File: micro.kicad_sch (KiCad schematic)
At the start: 29 parts, among them J7 USB_C_Receptacle_USB2.0_16P, J8 Conn_01x04_Pin, J9 Conn_01x06_Pin, SW2 SW_Push, U4 STM32F411RETx, U5 TME-0505S, U6 ADUM3160

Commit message: aggiunto oscillatore allo schematico
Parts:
- added C49, C50: 100n, Capacitor_SMD:C_0603_1608Metric, symbol Device:C
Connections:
- net +3V3: now also C49.1, C50.1
- net GND: now also C49.2, C50.2
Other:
- moved on the sheet: C45, C48, SW2

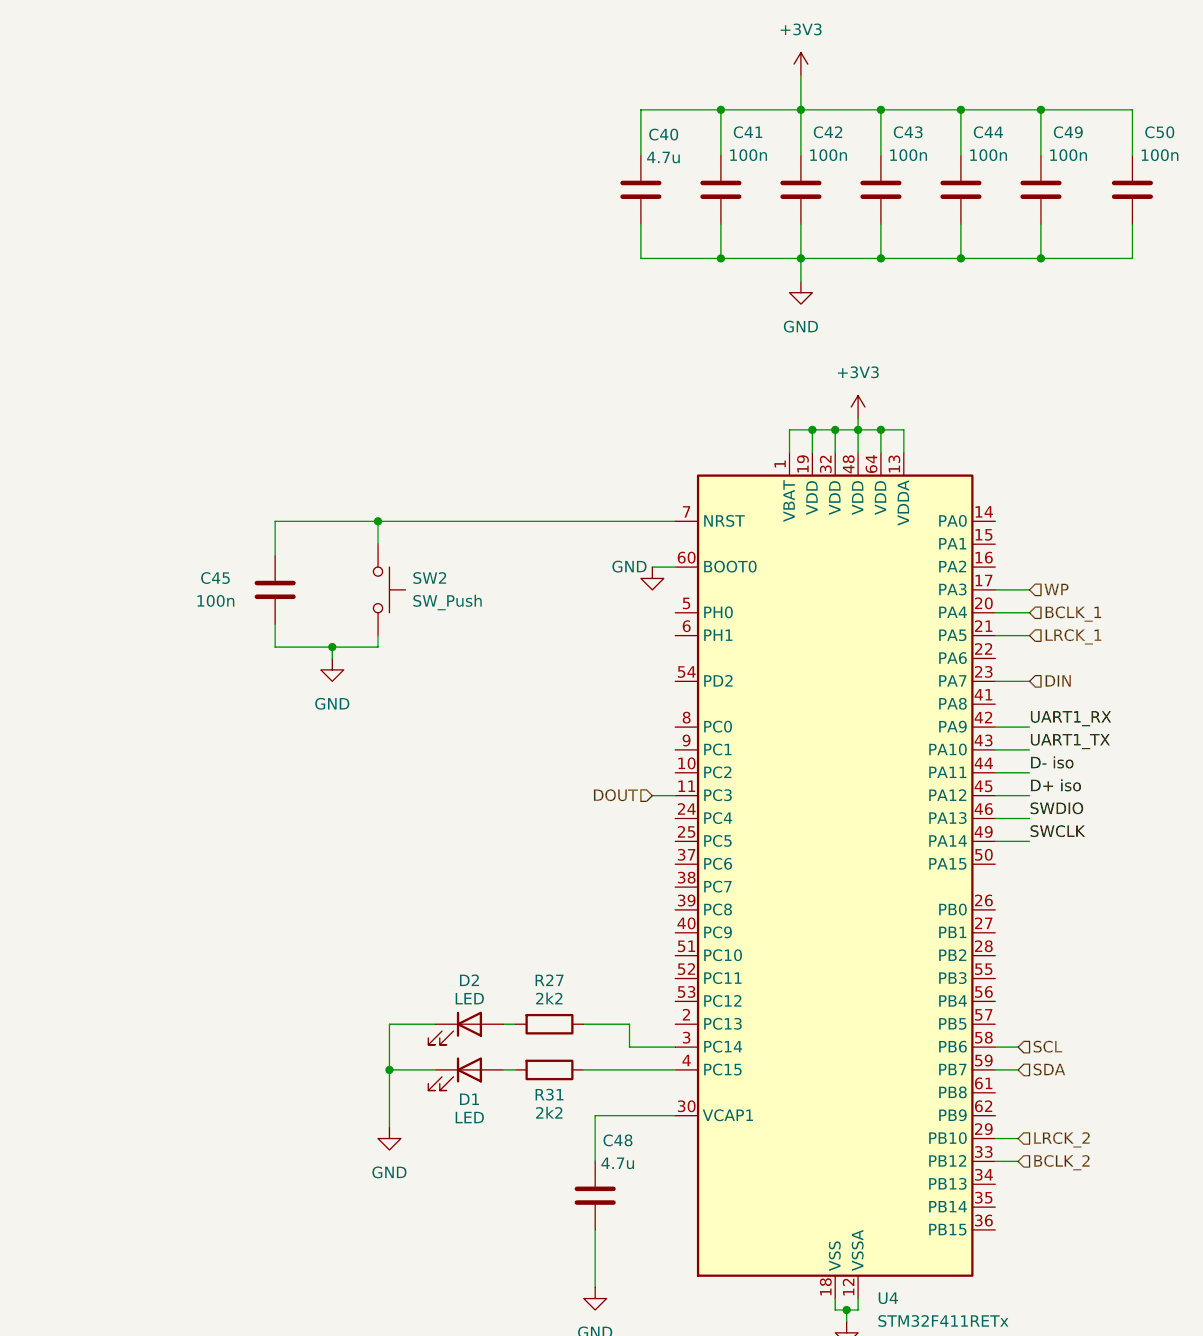
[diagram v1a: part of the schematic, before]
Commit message: sostituito dei componenti non piu disponibili
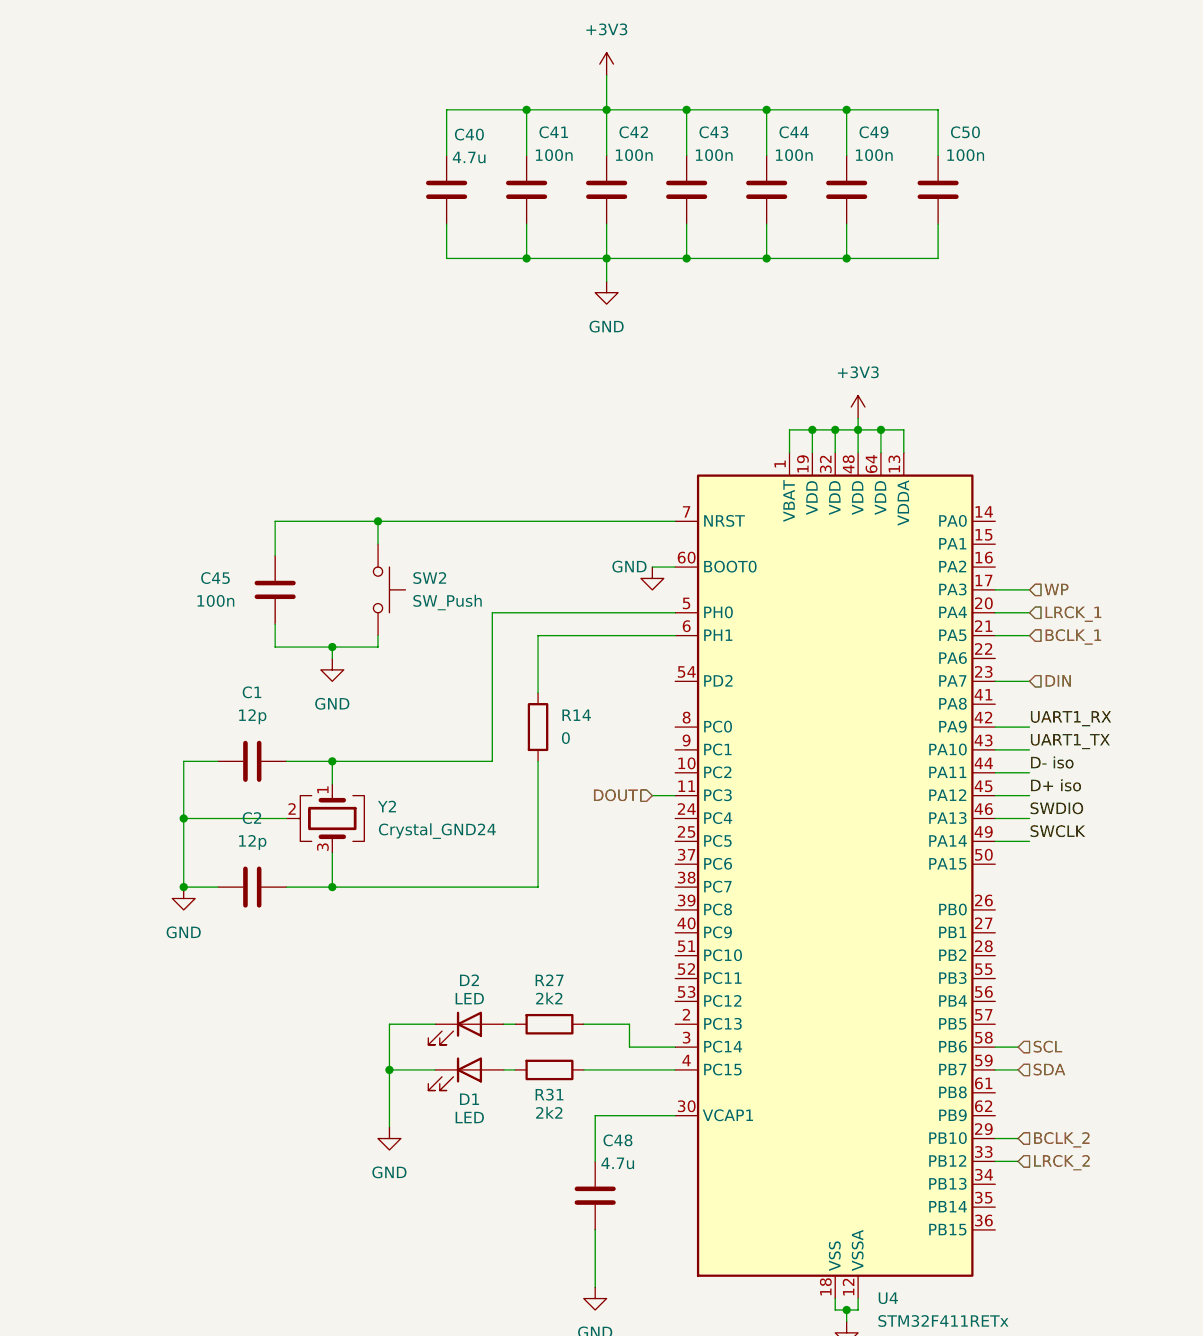
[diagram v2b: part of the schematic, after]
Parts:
- added C1, C2: 12p, Capacitor_SMD:C_0603_1608Metric, symbol Device:C
- added R14: 0, Resistor_SMD:R_0603_1608Metric, symbol Device:R
- added Y2: Crystal_GND24, Crystal:Crystal_SMD_3225-4Pin_3.2x2.5mm, symbol Device:Crystal_GND24
- J8: footprint Connector_JST:JST_XH_B4B-XH-AM_1x04_P2.50mm_Vertical -> Connector_JST:JST_XH_B4B-XH-A_1x04_P2.50mm_Vertical
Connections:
- net BCLK_1: now also U4.21 (PA5); no longer U4.20 (PA4)
- net BCLK_2: now also U4.29 (PB10); no longer U4.33 (PB12)
- net GND: now also C1.1, C2.1, Y2.2 (G), Y2.4 (G)
- net LRCK_1: now also U4.20 (PA4); no longer U4.21 (PA5)
- net LRCK_2: now also U4.33 (PB12); no longer U4.29 (PB10)
- net at U4.5 (PH0): now also C1.2, Y2.1
- net at U4.6 (PH1): now also R14.1
- new net: C2.2, R14.2, Y2.3
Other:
- moved on the sheet: C40, C41, C42, C43, C44, C49, C50

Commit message: modifiche suggerite da osti
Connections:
- no-connect marks 2 -> 32
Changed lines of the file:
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@@
 	)
 	(junction
-		(at 119.38 85.09)
-		(diameter 0)
-		(color 0 0 0 0)
-	)
-	(junction
 		(at 212.09 40.64)
 		(diameter 0)
@@
 	)
 	(junction
-		(at 121.92 72.39)
+		(at 251.46 59.69)
 		(diameter 0)
 		(color 0 0 0 0)
 	)
 	(junction
-		(at 251.46 59.69)
+		(at 124.46 72.39)
 		(diameter 0)
 		(color 0 0 0 0)
@@
 	)
 	(junction
+		(at 119.38 85.09)
+		(diameter 0)
+		(color 0 0 0 0)
+	)
+	(junction
 		(at 220.98 40.64)
 		(diameter 0)
@@
 	)
 	(no_connect
+		(at 228.6 102.87)
+	)
+	(no_connect
+		(at 228.6 92.71)
+	)
+	(no_connect
+		(at 264.16 120.65)
+	)
+	(no_connect
+		(at 228.6 107.95)
+	)
+	(no_connect
 		(at 53.34 66.04)
 	)
 	(no_connect
+		(at 264.16 133.35)
+	)
+	(no_connect
+		(at 228.6 120.65)
+	)
+	(no_connect
+		(at 228.6 97.79)
+	)
+	(no_connect
+		(at 264.16 85.09)
+	)
+	(no_connect
+		(at 228.6 123.19)
+	)
+	(no_connect
+		(at 264.16 143.51)
+	)
+	(no_connect
+		(at 264.16 69.85)
+	)
+	(no_connect
+		(at 264.16 72.39)
+	)
+	(no_connect
+		(at 264.16 125.73)
+	)
+	(no_connect
+		(at 264.16 115.57)
+	)
+	(no_connect
 		(at 53.34 68.58)
 	)
+	(no_connect
+		(at 264.16 107.95)
+	)
+	(no_connect
+		(at 264.16 113.03)
+	)
+	(no_connect
+		(at 228.6 95.25)
+	)
+	(no_connect
+		(at 228.6 105.41)
+	)
+	(no_connect
+		(at 264.16 135.89)
+	)
+	(no_connect
+		(at 228.6 110.49)
+	)
+	(no_connect
+		(at 228.6 87.63)
+	)
+	(no_connect
+		(at 228.6 125.73)
+	)
+	(no_connect
+		(at 228.6 118.11)
+	)
+	(no_connect
+		(at 264.16 118.11)
+	)
+	(no_connect
+		(at 228.6 113.03)
+	)
+	(no_connect
+		(at 264.16 74.93)
+	)
+	(no_connect
+		(at 264.16 148.59)
+	)
+	(no_connect
+		(at 264.16 123.19)
+	)
+	(no_connect
+		(at 264.16 146.05)
+	)
+	(no_connect
+		(at 228.6 115.57)
+	)
 	(wire
 		(pts
@@
 	(wire
 		(pts
-			(xy 114.3 69.85) (xy 121.92 69.85)
+			(xy 114.3 69.85) (xy 124.46 69.85)
 		)
 		(stroke
@@
 	(wire
 		(pts
-			(xy 125.73 85.09) (xy 119.38 85.09)
+			(xy 124.46 85.09) (xy 119.38 85.09)
 		)
 		(stroke
@@
 	(wire
 		(pts
-			(xy 121.92 72.39) (xy 125.73 72.39)
-		)
-		(stroke
-			(width 0)
-			(type default)
-		)
-	)
-	(wire
-		(pts
 			(xy 68.58 177.8) (xy 71.12 177.8)
 		)
@@
 	(wire
 		(pts
-			(xy 114.3 72.39) (xy 121.92 72.39)
+			(xy 114.3 72.39) (xy 124.46 72.39)
 		)
 		(stroke
@@
 	(wire
 		(pts
-			(xy 125.73 72.39) (xy 125.73 85.09)
+			(xy 124.46 72.39) (xy 124.46 85.09)
 		)
 		(stroke
@@
 	(wire
 		(pts
-			(xy 121.92 69.85) (xy 121.92 72.39)
+			(xy 124.46 69.85) (xy 124.46 72.39)
 		)
 		(stroke
@@
 		(in_pos_files yes)
 		(dnp no)
-		(fields_autoplaced yes)
 		(property "Reference" "C2"
-			(at 181.61 102.87 90)
+			(at 181.356 115.57 90)
 			(show_name no)
 			(do_not_autoplace no)
@@
 		)
 		(property "Value" "12p"
-			(at 181.61 105.41 90)
+			(at 181.356 118.11 90)
 			(show_name no)
 			(do_not_autoplace no)

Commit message: bom completata
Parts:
- C1, C2: value 12p -> 18p
- C48: footprint Capacitor_SMD:C_0603_1608Metric -> Capacitor_THT:C_Radial_D4.0mm_H7.0mm_P1.50mm
- Y2: value Crystal_GND24 -> 8M

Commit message: pulito lo schematico e fatto dei check
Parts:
- added R20, R23, R37, R38: 33, Resistor_SMD:R_0603_1608Metric, symbol Device:R
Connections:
- net D+: now also R23.1; no longer J7.A6 (D+), J7.B6 (D+)
- net D+ iso: now also R37.1; no longer U6.10 (DD+)
- net D-: now also R20.1; no longer J7.A7 (D-), J7.B7 (D-)
- net D- iso: now also R38.1; no longer U6.11 (DD-)
- new net: R38.2, U6.11 (DD-)
- new net: J7.A6 (D+), J7.B6 (D+), R23.2
- new net: J7.A7 (D-), J7.B7 (D-), R20.2
- new net: R37.2, U6.10 (DD+)
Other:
- note added: "Decupling capacitor bank"
- note added: "I2C Pullup Adau Eeprom programming"
- note added: "Isolator bypass jumper"
- note added: "Programming port"
- note added: "STM32F411"
- note added: "Usb Port + Usb Isolator"
- moved on the sheet: C1, C2, C30, C33, C36, C40, C41, C42, C43, C44, C45, C48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
